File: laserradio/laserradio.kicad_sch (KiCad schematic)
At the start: 75 parts, among them J1 USB4105-GF-A, J3 DEBUG, J4 RIGHT, U1 W25Q128JV, U2 RP2040, U3 MCP1702T-3302E_CB, U4 Opamp_Quad, U5 RS2255, U6 Opamp_Quad, Y1 12MHz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

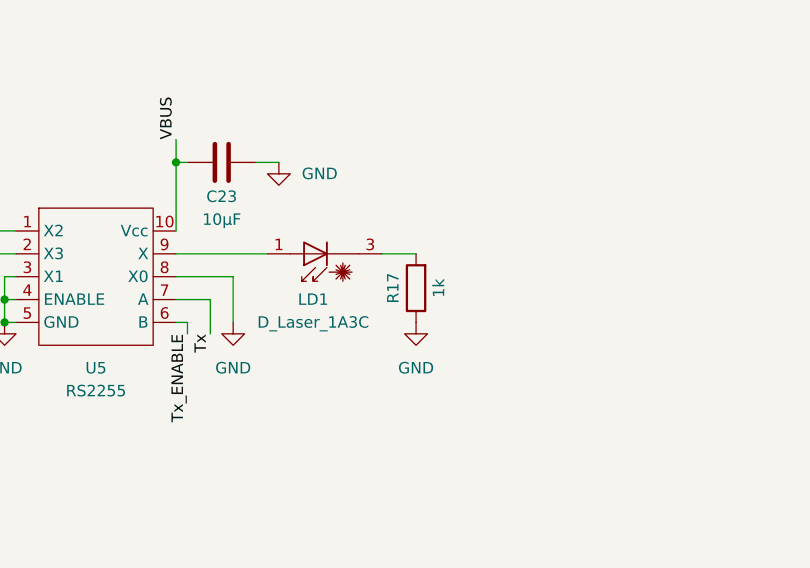
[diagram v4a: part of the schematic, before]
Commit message: Added laser switches
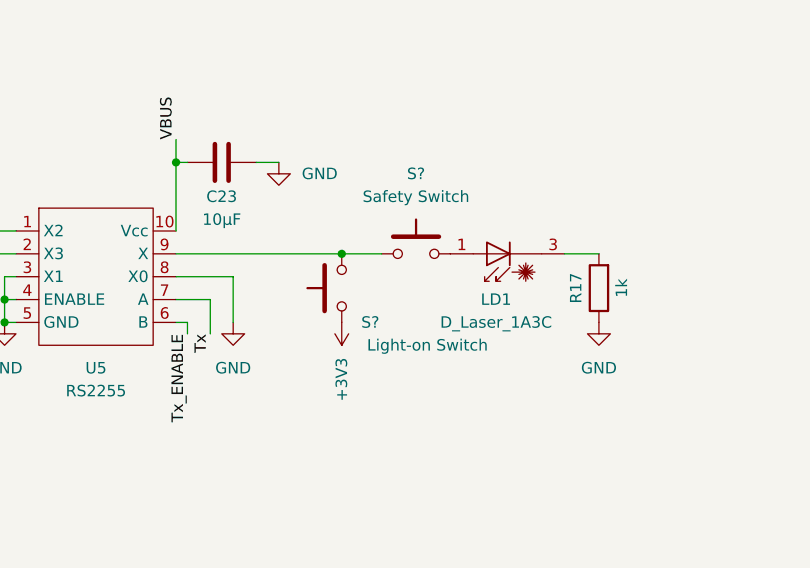
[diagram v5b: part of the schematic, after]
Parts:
- added S?: Safety Switch, symbol Eclectronics:SW
- added S?: Light-on Switch, symbol Eclectronics:SW
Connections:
- net +3V3: now also S?.1
- net at U5.9 (X): now also S?.1, S?.2; no longer LD1.1 (A)
- new net: LD1.1 (A), S?.2
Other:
- moved on the sheet: LD1, R17
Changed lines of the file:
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@@
   (junction (at 67.31 130.81) (diameter 0) (color 0 0 0 0)
   )
+  (junction (at 297.815 139.7) (diameter 0) (color 0 0 0 0)
+  )
   (junction (at 215.9 80.01) (diameter 0) (color 0 0 0 0)
   )
@@
     (stroke (width 0) (type default) (color 0 0 0 0))
   )
-  (wire (pts (xy 279.4 139.7) (xy 289.56 139.7))
+  (wire (pts (xy 279.4 139.7) (xy 297.815 139.7))
     (stroke (width 0) (type default) (color 0 0 0 0))
   )
@@
     (stroke (width 0) (type default) (color 0 0 0 0))
   )
-  (wire (pts (xy 302.26 139.7) (xy 306.07 139.7))
+  (wire (pts (xy 322.58 139.7) (xy 326.39 139.7))
     (stroke (width 0) (type default) (color 0 0 0 0))
   )
@@
     (stroke (width 0) (type default) (color 0 0 0 0))
   )
+  (wire (pts (xy 297.815 139.7) (xy 302.26 139.7))
+    (stroke (width 0) (type default) (color 0 0 0 0))
+  )
   (wire (pts (xy 78.74 181.61) (xy 80.01 181.61))
     (stroke (width 0) (type default) (color 0 0 0 0))
@@
     (pin "2")
   )
-  (symbol (lib_id "power:GND") (at 306.07 147.32 0) (unit 1)
+  (symbol (lib_id "power:GND") (at 326.39 147.32 0) (unit 1)
     (in_bom yes) (on_board yes) (fields_autoplaced)
-    (property "Reference" "#PWR046" (id 0) (at 306.07 153.67 0)
+    (property "Reference" "#PWR046" (id 0) (at 326.39 153.67 0)
       (effects (font (size 1.27 1.27)) hide)
     )
-    (property "Value" "GND" (id 1) (at 306.07 152.4 0))
-    (property "Footprint" "" (id 2) (at 306.07 147.32 0)
+    (property "Value" "GND" (id 1) (at 326.39 152.4 0))
+    (property "Footprint" "" (id 2) (at 326.39 147.32 0)
       (effects (font (size 1.27 1.27)) hide)
     )
-    (property "Datasheet" "" (id 3) (at 306.07 147.32 0)
+    (property "Datasheet" "" (id 3) (at 326.39 147.32 0)
       (effects (font (size 1.27 1.27)) hide)
     )
@@
     (pin "1")
   )
+  (symbol (lib_id "Eclectronics:SW") (at 306.07 139.7 270) (unit 1)
+    (in_bom yes) (on_board yes) (fields_autoplaced)
+    (property "Reference" "S?" (id 0) (at 306.07 130.81 90))
+    (property "Value" "Safety Switch" (id 1) (at 306.07 133.35 90))
+    (property "Footprint" "" (id 2) (at 308.61 140.97 90)
+      (effects (font (size 1.524 1.524)) hide)
+    )
+    (property "Datasheet" "" (id 3) (at 308.61 140.97 90)
+      (effects (font (size 1.524 1.524)) hide)
+    )
+    (pin "1")
+    (pin "2")
+  )
   (symbol (lib_id "Device:C") (at 177.8 29.21 0) (mirror x) (unit 1)
     (in_bom yes) (on_board yes) (fields_autoplaced)
@@
     (pin "2")
   )
+  (symbol (lib_id "Eclectronics:SW") (at 297.815 143.51 0) (unit 1)
+    (in_bom yes) (on_board yes)
+    (property "Reference" "S?" (id 0) (at 300.99 147.32 0))
+    (property "Value" "Light-on Switch" (id 1) (at 307.34 149.86 0))
+    (property "Footprint" "" (id 2) (at 299.085 140.97 90)
+      (effects (font (size 1.524 1.524)) hide)
+    )
+    (property "Datasheet" "" (id 3) (at 299.085 140.97 90)
+      (effects (font (size 1.524 1.524)) hide)
+    )
+    (pin "1")
+    (pin "2")
+  )
   (symbol (lib_id "power:GND") (at 306.07 86.36 0) (unit 1)
     (in_bom yes) (on_board yes)
@@
     (pin "2")
   )
-  (symbol (lib_id "Device:R") (at 306.07 143.51 180) (unit 1)
+  (symbol (lib_id "Device:R") (at 326.39 143.51 180) (unit 1)
     (in_bom yes) (on_board yes)
-    (property "Reference" "R17" (id 0) (at 303.53 143.51 90))
-    (property "Value" "1k" (id 1) (at 308.61 143.51 90))
-    (property "Footprint" "Resistor_SMD:R_0402_1005Metric" (id 2) (at 307.848 143.51 90)
+    (property "Reference" "R17" (id 0) (at 323.85 143.51 90))
+    (property "Value" "1k" (id 1) (at 328.93 143.51 90))
+    (property "Footprint" "Resistor_SMD:R_0402_1005Metric" (id 2) (at 328.168 143.51 90)
       (effects (font (size 1.27 1.27)) hide)
     )
-    (property "Datasheet" "~" (id 3) (at 306.07 143.51 0)
+    (property "Datasheet" "~" (id 3) (at 326.39 143.51 0)
       (effects (font (size 1.27 1.27)) hide)
     )
@@
     (pin "1")
   )
+  (symbol (lib_id "power:+3V3") (at 297.815 147.32 180) (unit 1)
+    (in_bom yes) (on_board yes)
+    (property "Reference" "#PWR?" (id 0) (at 297.815 143.51 0)
+      (effects (font (size 1.27 1.27)) hide)
+    )
+    (property "Value" "+3V3" (id 1) (at 297.815 153.67 90))
+    (property "Footprint" "" (id 2) (at 297.815 147.32 0)
+      (effects (font (size 1.27 1.27)) hide)
+    )
+    (property "Datasheet" "" (id 3) (at 297.815 147.32 0)
+      (effects (font (size 1.27 1.27)) hide)
+    )
+    (pin "1")
+  )
   (symbol (lib_id "power:GND") (at 193.04 177.165 0) (unit 1)
     (in_bom yes) (on_board yes) (fields_autoplaced)
@@
     (pin "2")
   )
-  (symbol (lib_id "Device:D_Laser_1A3C") (at 294.64 139.7 180) (unit 1)
+  (symbol (lib_id "Device:D_Laser_1A3C") (at 314.96 139.7 180) (unit 1)
     (in_bom yes) (on_board yes)
-    (property "Reference" "LD1" (id 0) (at 294.64 144.78 0))
-    (property "Value" "D_Laser_1A3C" (id 1) (at 294.64 147.32 0))
-    (property "Footprint" "" (id 2) (at 297.18 139.065 0)
+    (property "Reference" "LD1" (id 0) (at 314.96 144.78 0))
+    (property "Value" "D_Laser_1A3C" (id 1) (at 314.96 147.32 0))
+    (property "Footprint" "" (id 2) (at 317.5 139.065 0)
       (effects (font (size 1.27 1.27)) hide)
     )
-    (property "Datasheet" "~" (id 3) (at 293.878 134.62 0)
+    (property "Datasheet" "~" (id 3) (at 314.198 134.62 0)
       (effects (font (size 1.27 1.27)) hide)
     )
@@
       (reference "#PWR?") (unit 1) (value "GND") (footprint "")
     )
+    (path "/cda02c27-7071-435a-ae7e-26c88efacb1d"
+      (reference "#PWR?") (unit 1) (value "+3V3") (footprint "")
+    )
     (path "/ce41a605-9e8d-45b2-ad67-14bd4ff341aa"
       (reference "#PWR?") (unit 1) (value "GND") (footprint "")
@@
       (reference "S2") (unit 1) (value "BOOT") (footprint "Eclectronics:KXT321LHS")
     )
+    (path "/716a88af-5dbc-4392-bd15-d7b62d509d38"
+      (reference "S?") (unit 1) (value "Safety Switch") (footprint "")
+    )
+    (path "/9c2d29cd-1aec-4011-acd1-d66c1139a818"
+      (reference "S?") (unit 1) (value "Light-on Switch") (footprint "")
+    )
     (path "/93837370-9890-4ba1-9c48-cd8c2201b210"

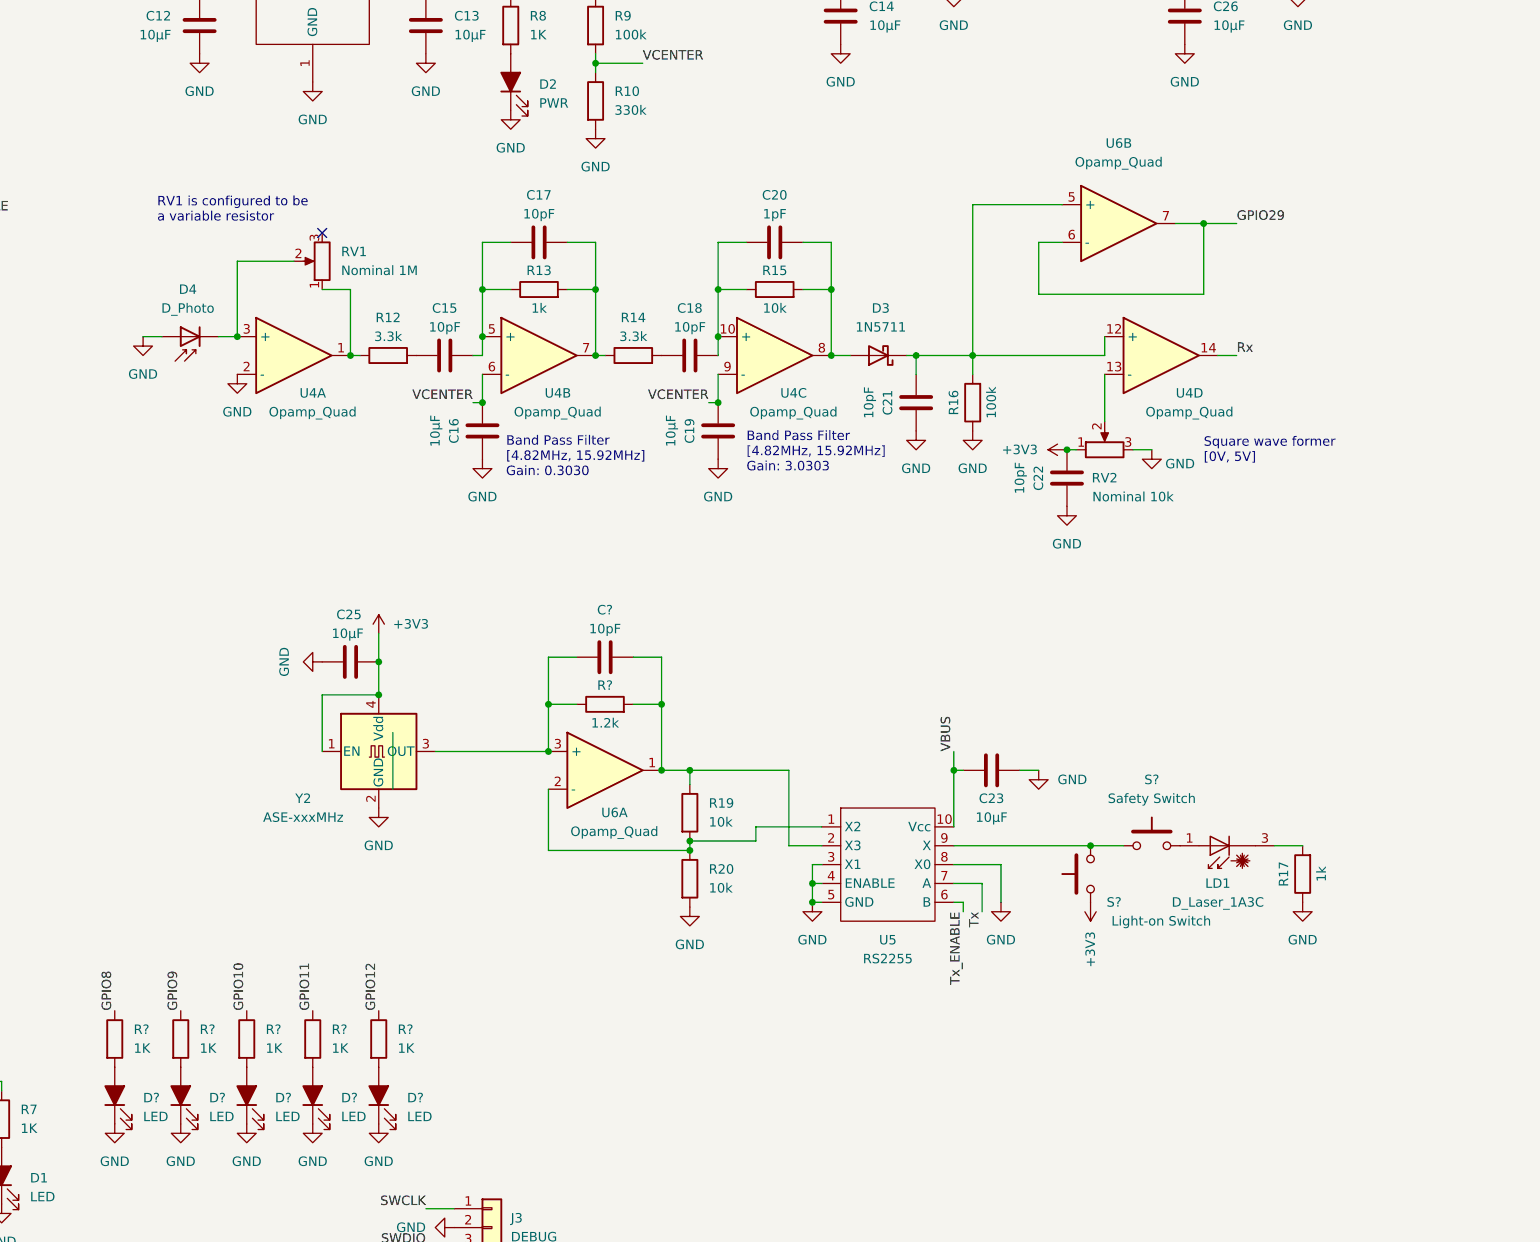
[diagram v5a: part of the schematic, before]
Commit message: change switches and add annotations
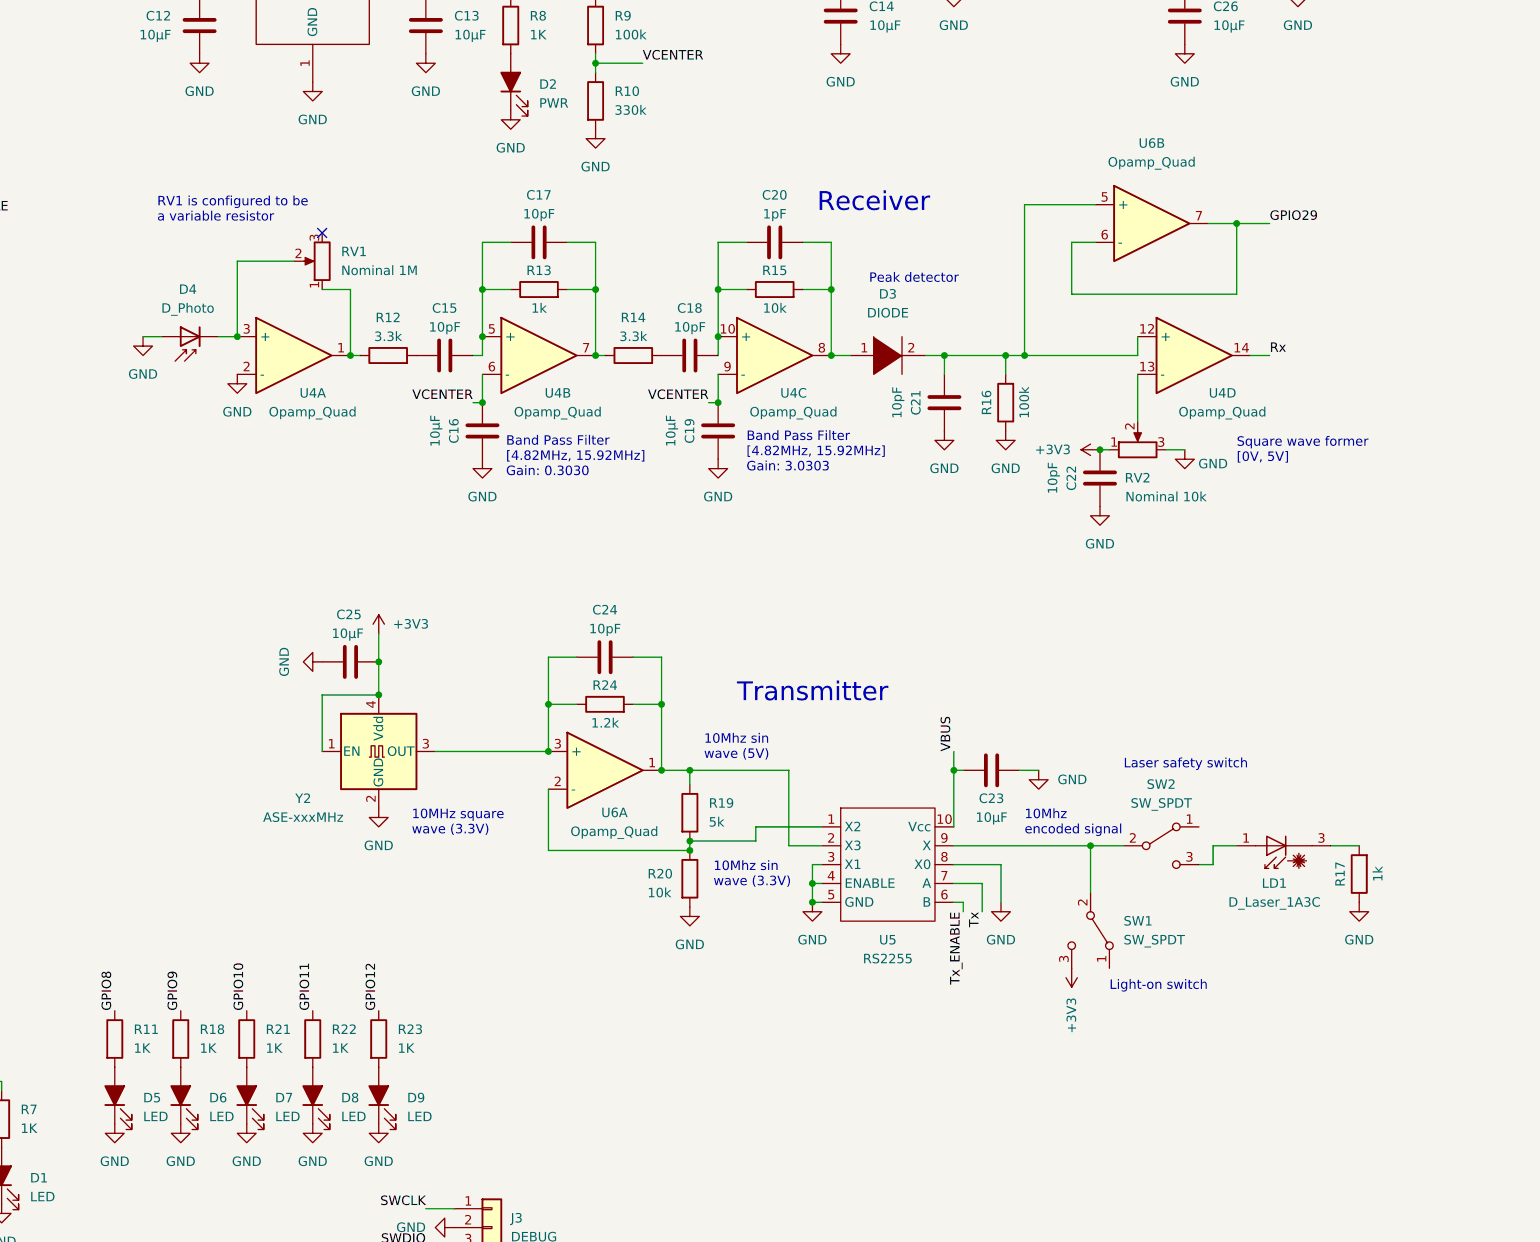
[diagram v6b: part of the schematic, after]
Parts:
- removed D3: 1N5711, Diode_THT:D_DO-35_SOD27_P7.62mm_Horizontal, symbol Diode:1N5711
- removed S?: Safety Switch, symbol Eclectronics:SW
- removed S?: Light-on Switch, symbol Eclectronics:SW
- added D3: DIODE, symbol pspice:DIODE
- added SW1, SW2: SW_SPDT, symbol Switch:SW_SPDT
- R19: value 10k -> 5k
- gave numbers to parts that had none: 12
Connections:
- net +3V3: now also SW1.3 (C)
- net at C21.1, R16.2, U4.12 (+)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: now also D3.2 (A)
- net at C20.2, R15.2, U4.8: now also D3.1 (K)
- net at U5.9 (X): now also SW1.2 (B), SW2.2 (B)
- net at LD1.1 (A): now also SW2.3 (C)
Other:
- note added: "10MHz square wave (3.3V)"
- note added: "10Mhz encoded signal"
- note added: "10Mhz sin wave (3.3V)"
- note added: "10Mhz sin wave (5V)"
- note added: "Laser safety switch"
- note added: "Light-on switch"
- note added: "Peak detector"
- note added: "Receiver"
- note added: "Transmitter"
- moved on the sheet: C21, C22, LD1, R16, R17, RV2, U4D, U6B
